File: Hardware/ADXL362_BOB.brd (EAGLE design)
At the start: 12.7 x 10.2 mm, 9 parts, among them U1 ADXL362

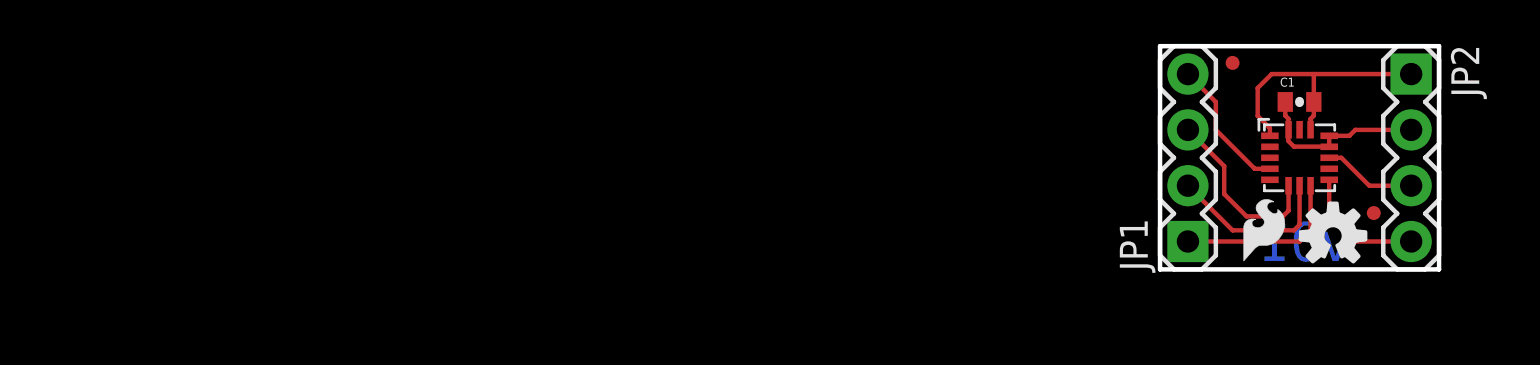
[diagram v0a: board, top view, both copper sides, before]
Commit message: Moved to 0603, Traces, 1:1
1:1 on the Adxl362
Minor trace re-route
cap moved to 0603
Sch update
Rev #1 update
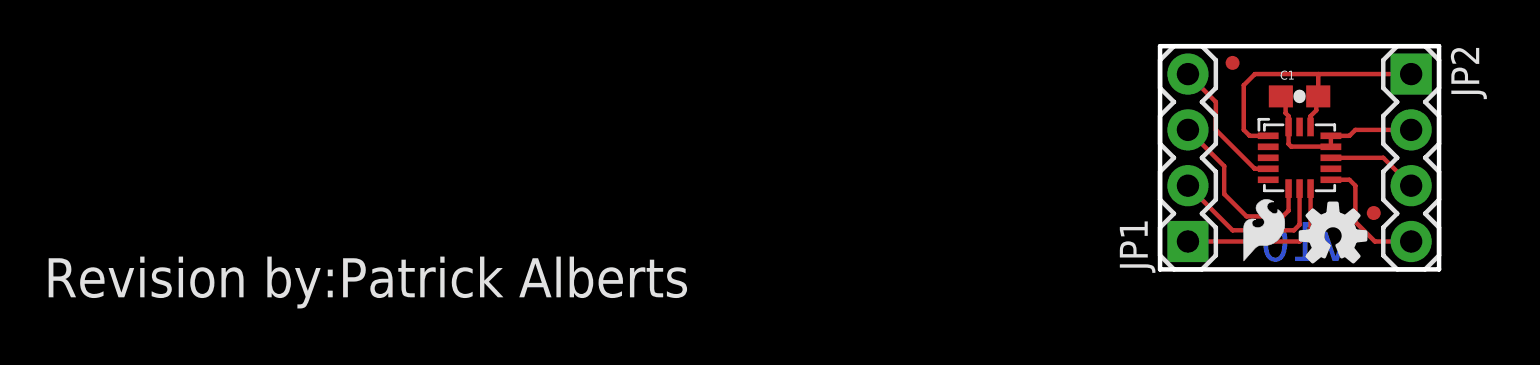
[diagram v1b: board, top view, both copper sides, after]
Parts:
- C1: device SparkFun-Passives:0402-CAP -> SparkFun-Capacitors:0603-CAP
- U1: value ADXL362 -> (none); device SparkFun-Sensors:ADXL362 -> SparkFun-Sensors:ADXL362-1:1
- moved C1 0.25 mm to (6.35, 7.87)
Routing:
- net 3.3V: track 12.3 -> 13.6 mm
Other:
- board text added: "Revision by:Patrick Alberts"
- board text added: "v10"
- board text removed: "v01"

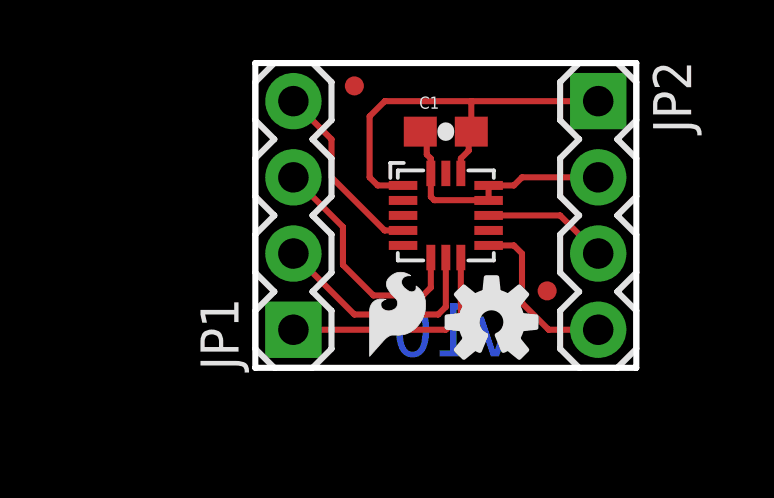
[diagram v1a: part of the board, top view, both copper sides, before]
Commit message: changed fiducials from micro to regular
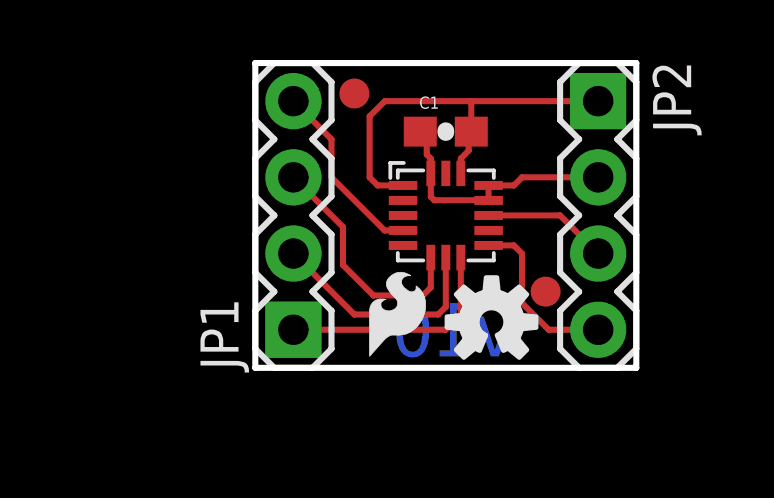
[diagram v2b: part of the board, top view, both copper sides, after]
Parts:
- removed JP4, JP5: FIDUCIALUFIDUCIAL, SparkFun:MICRO-FIDUCIAL
- added FID1, FID2: FIDUCIAL1X2, SparkFun-Aesthetics:FIDUCIAL-1X2
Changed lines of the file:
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@@
 <?xml version="1.0" encoding="utf-8"?>
 <!DOCTYPE eagle SYSTEM "eagle.dtd">
-<eagle version="6.4">
+<eagle version="6.5.0">
 <drawing>
 <settings>
@@
 <setting verticaltext="up"/>
 </settings>
-<grid distance="0.05" unitdist="inch" unit="inch" style="lines" multiple="1" display="yes" altdistance="0.005" altunitdist="inch" altunit="inch"/>
+<grid distance="0.01" unitdist="inch" unit="inch" style="lines" multiple="1" display="yes" altdistance="0.001" altunitdist="inch" altunit="inch"/>
 <layers>
 <layer number="1" name="Top" color="4" fill="1" visible="yes" active="yes"/>
@@
 <layer number="18" name="Vias" color="2" fill="1" visible="yes" active="yes"/>
 <layer number="19" name="Unrouted" color="6" fill="1" visible="yes" active="yes"/>
-<layer number="20" name="Dimension" color="15" fill="1" visible="yes" active="yes"/>
-<layer number="21" name="tPlace" color="16" fill="1" visible="yes" active="yes"/>
-<layer number="22" name="bPlace" color="14" fill="1" visible="yes" active="yes"/>
+<layer number="20" name="Dimension" color="6" fill="1" visible="yes" active="yes"/>
+<layer number="21" name="tPlace" color="6" fill="1" visible="yes" active="yes"/>
+<layer number="22" name="bPlace" color="6" fill="1" visible="yes" active="yes"/>
 <layer number="23" name="tOrigins" color="15" fill="1" visible="yes" active="yes"/>
 <layer number="24" name="bOrigins" color="15" fill="1" visible="yes" active="yes"/>
@@
 <element name="U$1" library="SparkFun-Aesthetics" package="OSHW-LOGO-S" value="OSHW-LOGOS" x="7.874" y="1.524"/>
 <element name="FRAME1" library="SparkFun-Aesthetics" package="CREATIVE_COMMONS" value="FRAME-LETTER" x="-77.47" y="1.27"/>
-<element name="JP4" library="SparkFun" package="MICRO-FIDUCIAL" value="FIDUCIALUFIDUCIAL" x="3.302" y="9.398"/>
-<element name="JP5" library="SparkFun" package="MICRO-FIDUCIAL" value="FIDUCIALUFIDUCIAL" x="9.7282" y="2.5654"/>
+<element name="FID1" library="SparkFun-Aesthetics" package="FIDUCIAL-1X2" value="FIDUCIAL1X2" x="3.302" y="9.144"/>
+<element name="FID2" library="SparkFun-Aesthetics" package="FIDUCIAL-1X2" value="FIDUCIAL1X2" x="9.6774" y="2.54"/>
 </elements>
 <signals>
